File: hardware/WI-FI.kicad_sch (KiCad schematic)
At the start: 17 parts

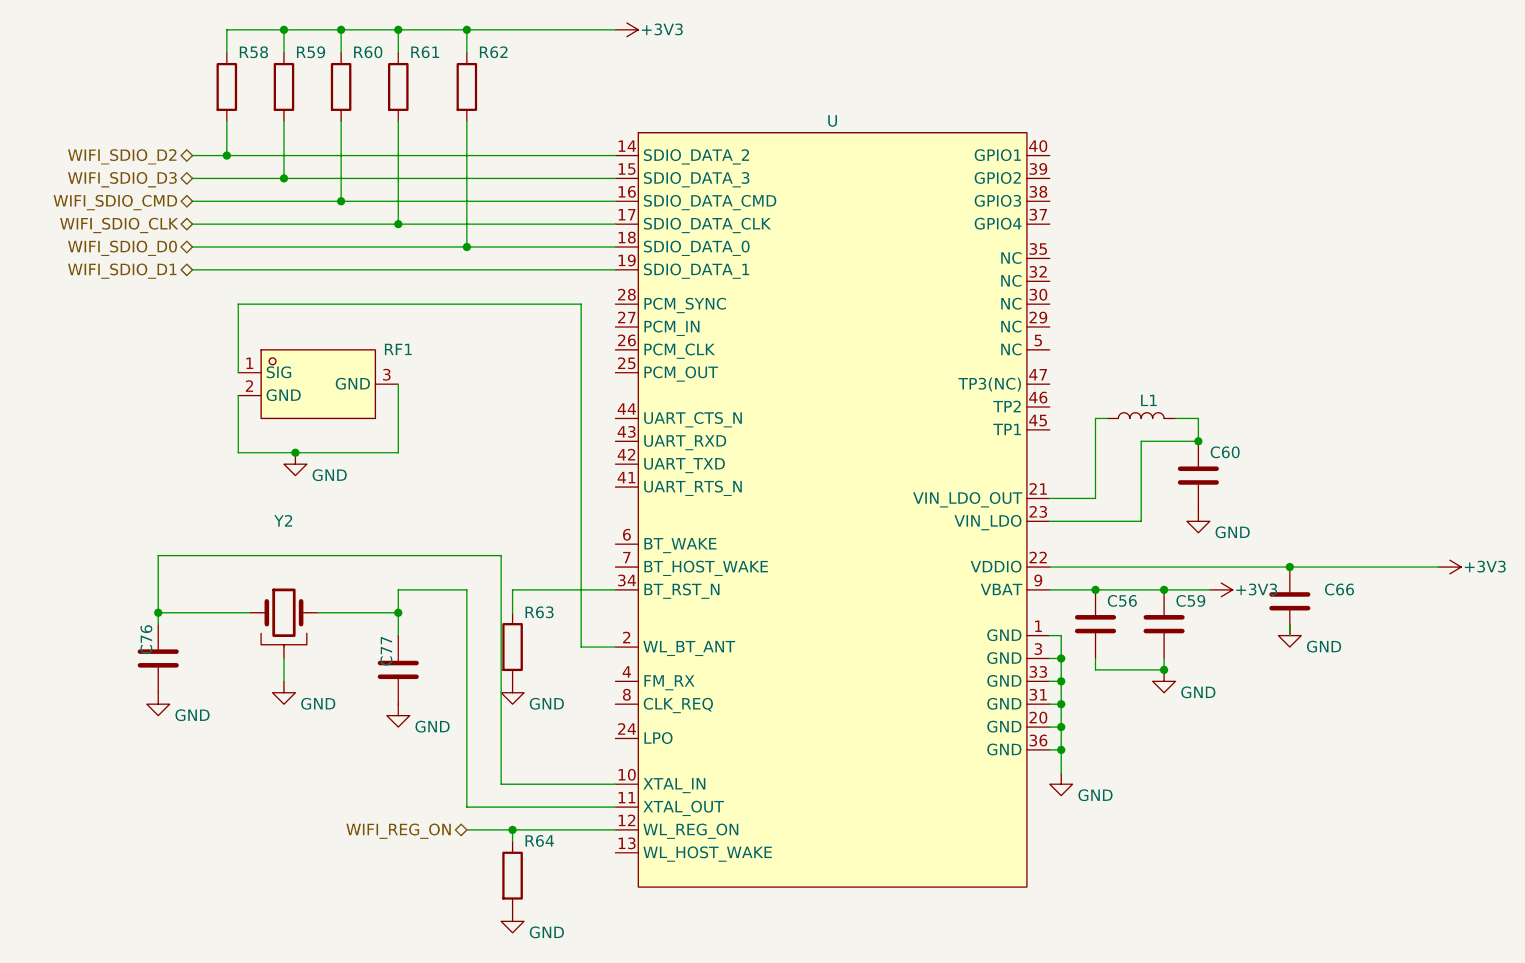
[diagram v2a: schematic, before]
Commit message: ferrite bead in adc power net is added
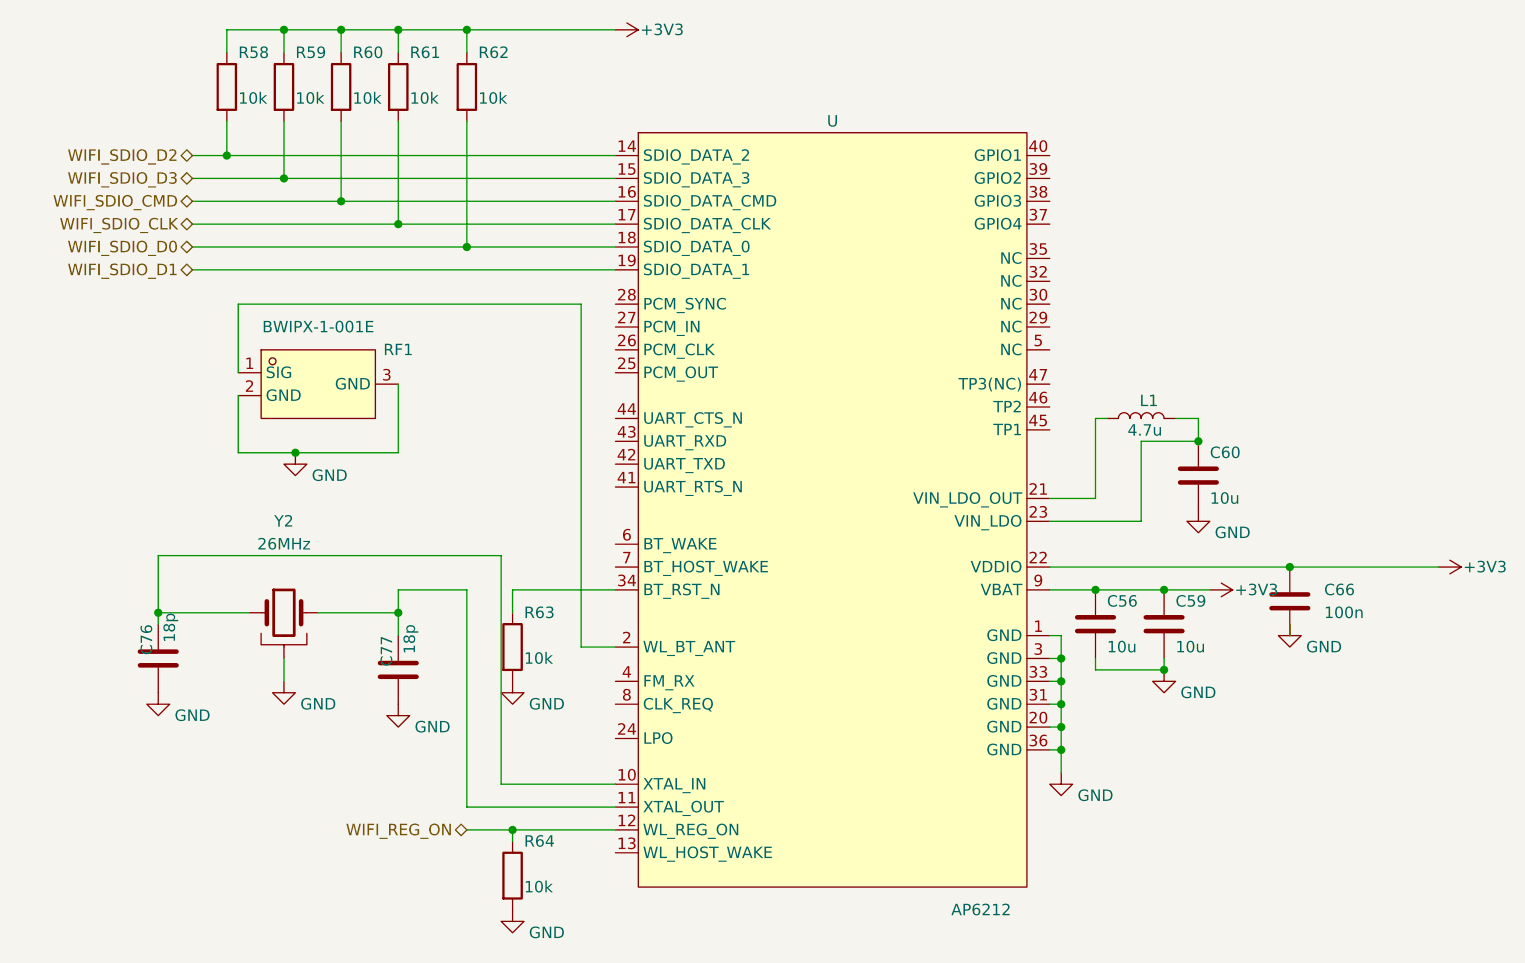
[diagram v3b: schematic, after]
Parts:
- C56, C59, C60: value (none) -> 10u
- C66: value (none) -> 100n
- C76, C77: value (none) -> 18p
- L1: value (none) -> 4.7u
- R58, R59, R60, R61, R62, R63, R64: value (none) -> 10k
- RF1: value (none) -> BWIPX-1-001E
- Y2: value (none) -> 26МHz
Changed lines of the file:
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@@
       (effects (font (size 1.27 1.27)) (justify left))
     )
-    (property "Value" "" (id 1) (at 111.76 105.41 0)
+    (property "Value" "10k" (id 1) (at 111.76 105.41 0)
       (effects (font (size 1.27 1.27)) (justify left))
     )
@@
       (effects (font (size 1.27 1.27)) (justify left))
     )
-    (property "Value" "" (id 1) (at 111.76 130.81 0)
+    (property "Value" "10k" (id 1) (at 111.76 130.81 0)
       (effects (font (size 1.27 1.27)) (justify left))
     )
@@
     (in_bom yes) (on_board yes)
     (property "Reference" "U12" (id 0) (at 146.05 45.72 0))
-    (property "Value" "" (id 1) (at 162.56 133.35 0))
+    (property "Value" "AP6212" (id 1) (at 162.56 133.35 0))
     (property "Footprint" "" (id 2) (at 146.05 115.57 0)
       (effects (font (size 1.27 1.27)) hide)
@@
     (in_bom yes) (on_board yes)
     (property "Reference" "RF1" (id 0) (at 97.79 71.12 0))
-    (property "Value" "" (id 1) (at 88.9 68.58 0))
+    (property "Value" "BWIPX-1-001E" (id 1) (at 88.9 68.58 0))
     (property "Footprint" "" (id 2) (at 88.9 83.82 0)
       (effects (font (size 1.27 1.27)) hide)
@@
     (in_bom yes) (on_board yes)
     (property "Reference" "Y2" (id 0) (at 85.09 90.17 0))
-    (property "Value" "" (id 1) (at 85.09 92.71 0))
+    (property "Value" "26МHz" (id 1) (at 85.09 92.71 0))
     (property "Footprint" "" (id 2) (at 83.82 118.11 0))
     (property "Datasheet" "~" (id 3) (at 95.25 113.03 0)
@@
       (effects (font (size 1.27 1.27)) (justify left))
     )
-    (property "Value" "" (id 1) (at 200.66 100.3299 0)
+    (property "Value" "100n" (id 1) (at 200.66 100.3299 0)
       (effects (font (size 1.27 1.27)) (justify left))
     )
@@
       (effects (font (size 1.27 1.27)) (justify left))
     )
-    (property "Value" "" (id 1) (at 184.15 104.14 0)
+    (property "Value" "10u" (id 1) (at 184.15 104.14 0)
       (effects (font (size 1.27 1.27)) (justify left))
     )
@@
     (in_bom yes) (on_board yes)
     (property "Reference" "L1" (id 0) (at 181.1924 76.7822 90))
-    (property "Value" "" (id 1) (at 180.7551 80.0615 90))
+    (property "Value" "4.7u" (id 1) (at 180.7551 80.0615 90))
     (property "Footprint" "" (id 2) (at 180.34 78.74 0)
       (effects (font (size 1.27 1.27)) hide)
@@
       (effects (font (size 1.27 1.27)) (justify left))
     )
-    (property "Value" "" (id 1) (at 86.36 43.18 0)
+    (property "Value" "10k" (id 1) (at 86.36 43.18 0)
       (effects (font (size 1.27 1.27)) (justify left))
     )
@@
       (effects (font (size 1.27 1.27)) (justify left))
     )
-    (property "Value" "" (id 1) (at 106.68 43.18 0)
+    (property "Value" "10k" (id 1) (at 106.68 43.18 0)
       (effects (font (size 1.27 1.27)) (justify left))
     )
@@
       (effects (font (size 1.27 1.27)) (justify left))
     )
-    (property "Value" "" (id 1) (at 176.53 104.14 0)
+    (property "Value" "10u" (id 1) (at 176.53 104.14 0)
       (effects (font (size 1.27 1.27)) (justify left))
     )
@@
       (effects (font (size 1.27 1.27)) (justify left))
     )
-    (property "Value" "" (id 1) (at 99.06 43.18 0)
+    (property "Value" "10k" (id 1) (at 99.06 43.18 0)
       (effects (font (size 1.27 1.27)) (justify left))
     )
@@
       (effects (font (size 1.27 1.27)) (justify left))
     )
-    (property "Value" "" (id 1) (at 187.96 87.63 0)
+    (property "Value" "10u" (id 1) (at 187.96 87.63 0)
       (effects (font (size 1.27 1.27)) (justify left))
     )
@@
       (effects (font (size 1.27 1.27)) (justify left))
     )
-    (property "Value" "" (id 1) (at 99.06 101.6 90)
+    (property "Value" "18p" (id 1) (at 99.06 101.6 90)
       (effects (font (size 1.27 1.27)) (justify left))
     )
@@
       (effects (font (size 1.27 1.27)) (justify left))
     )
-    (property "Value" "" (id 1) (at 80.01 43.18 0)
+    (property "Value" "10k" (id 1) (at 80.01 43.18 0)
       (effects (font (size 1.27 1.27)) (justify left))
     )
@@
       (effects (font (size 1.27 1.27)) (justify left))
     )
-    (property "Value" "" (id 1) (at 92.71 43.18 0)
+    (property "Value" "10k" (id 1) (at 92.71 43.18 0)
       (effects (font (size 1.27 1.27)) (justify left))
     )
@@
       (effects (font (size 1.27 1.27)) (justify left))
     )
-    (property "Value" "" (id 1) (at 72.39 100.33 90)
-      (effects (font (size 1.27 1.27)) (justify left))
-    )
+    (property "Value" "18p" (id 1) (at 72.39 100.33 90)
+      (effects (font (size 1.27 1.27)) (justify left))
+    )
